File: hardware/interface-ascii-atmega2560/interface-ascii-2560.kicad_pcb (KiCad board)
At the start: 2 copper layers, 88.9 x 132.1 mm, 50 parts, among them J1 Apple 2, J10 Keyboard, J2 Apple 1, J3 UART, J4 Conn_01x05, J5 SOL-20, J6 Program, J7 Custom Connector 1 / Proto, J8 Conn_01x25, SW1 Options, U1 ATmega2560-16AU, Y1 16.000 MHz

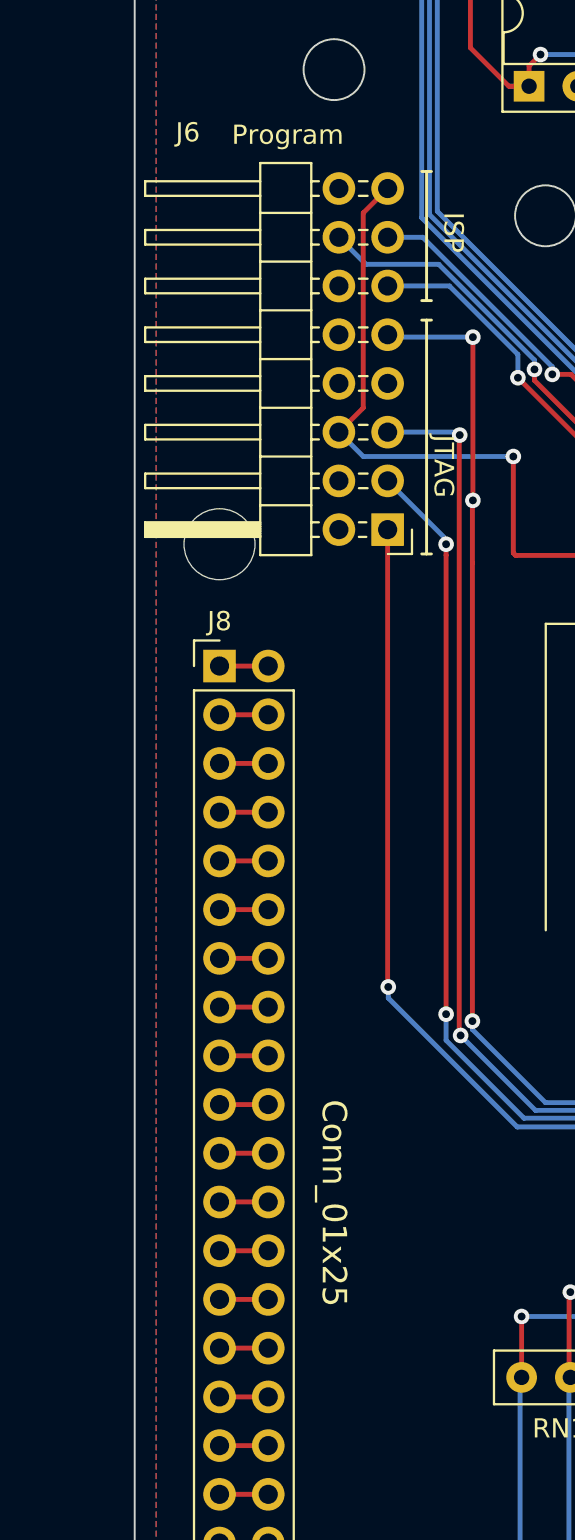
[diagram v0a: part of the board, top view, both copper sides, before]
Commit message: Fix connector J8 name to "custom connector 2"
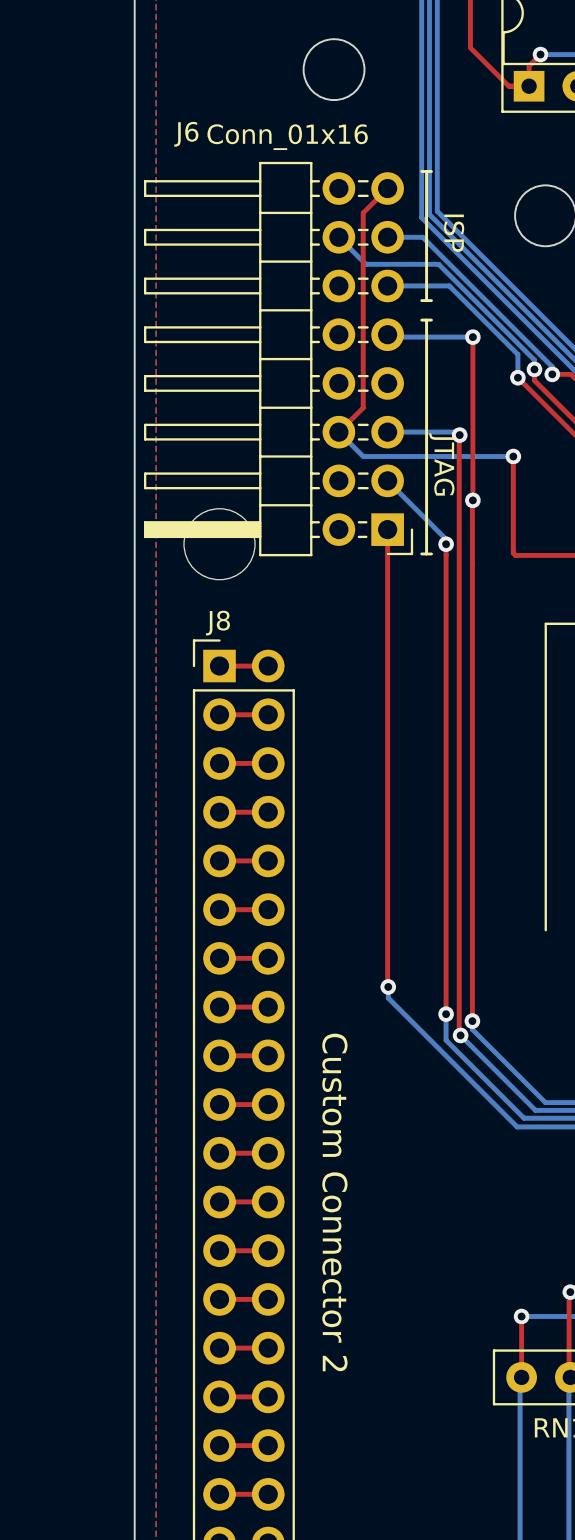
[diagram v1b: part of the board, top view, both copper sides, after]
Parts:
- J6: value Program -> Conn_01x16
- J8: value Conn_01x25 -> Custom Connector 2
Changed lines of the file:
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@@
       (effects (font (size 1 1) (thickness 0.15)))
     )
-    (fp_text value Program (at 5.207 20.574) (layer F.SilkS)
+    (fp_text value Conn_01x16 (at 5.207 20.574) (layer F.SilkS)
       (effects (font (size 1 1) (thickness 0.15)))
     )
@@
       (effects (font (size 1 1) (thickness 0.15)))
     )
-    (fp_text value Conn_01x25 (at 5.969 28.0035 270 unlocked) (layer F.SilkS)
+    (fp_text value "Custom Connector 2" (at 5.969 28.0035 270 unlocked) (layer F.SilkS)
       (effects (font (size 1.27 1.27) (thickness 0.15)))
     )

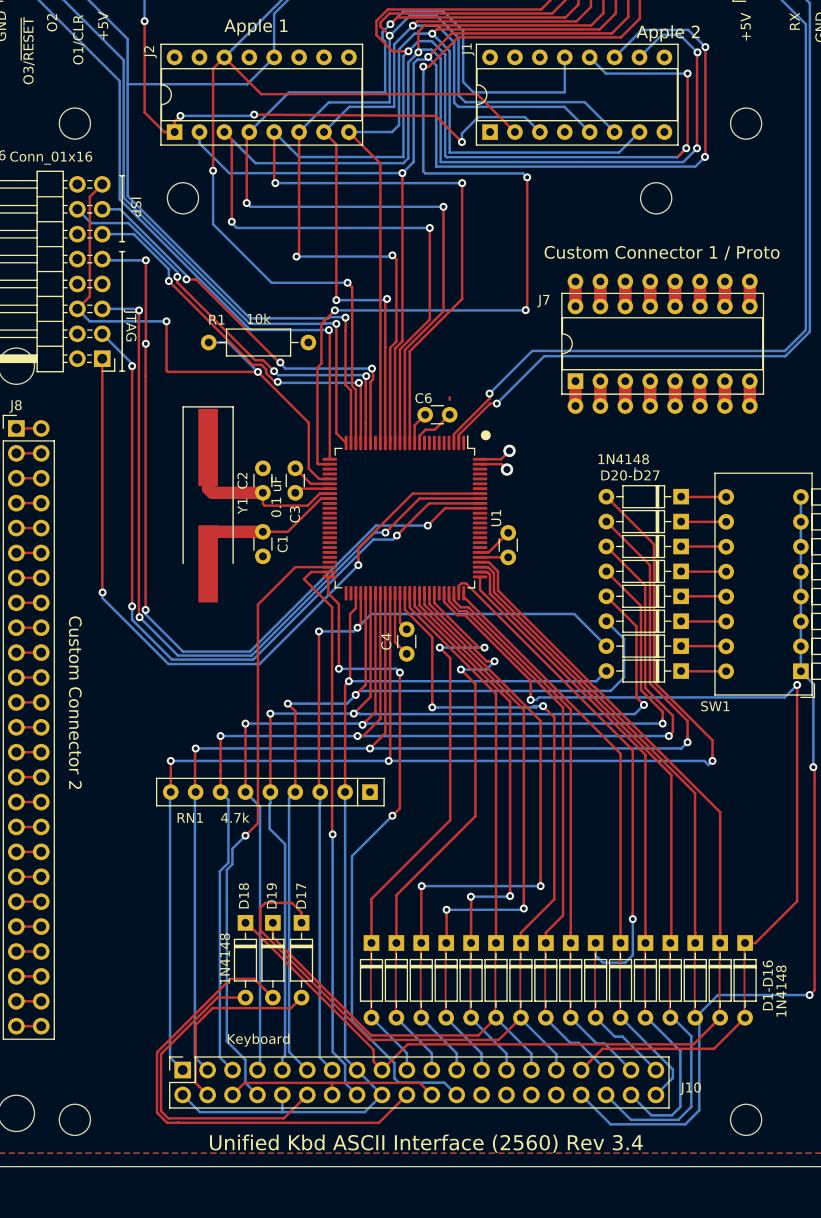
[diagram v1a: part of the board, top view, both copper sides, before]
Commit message: mechanical fit and buildability fixes
- Moved header slightly forward

- Moved interface mount holes do reduce interference with case mount holes

- For all keys in classic keyboard, add option for either through-hole or SMT
diodes and resistors.
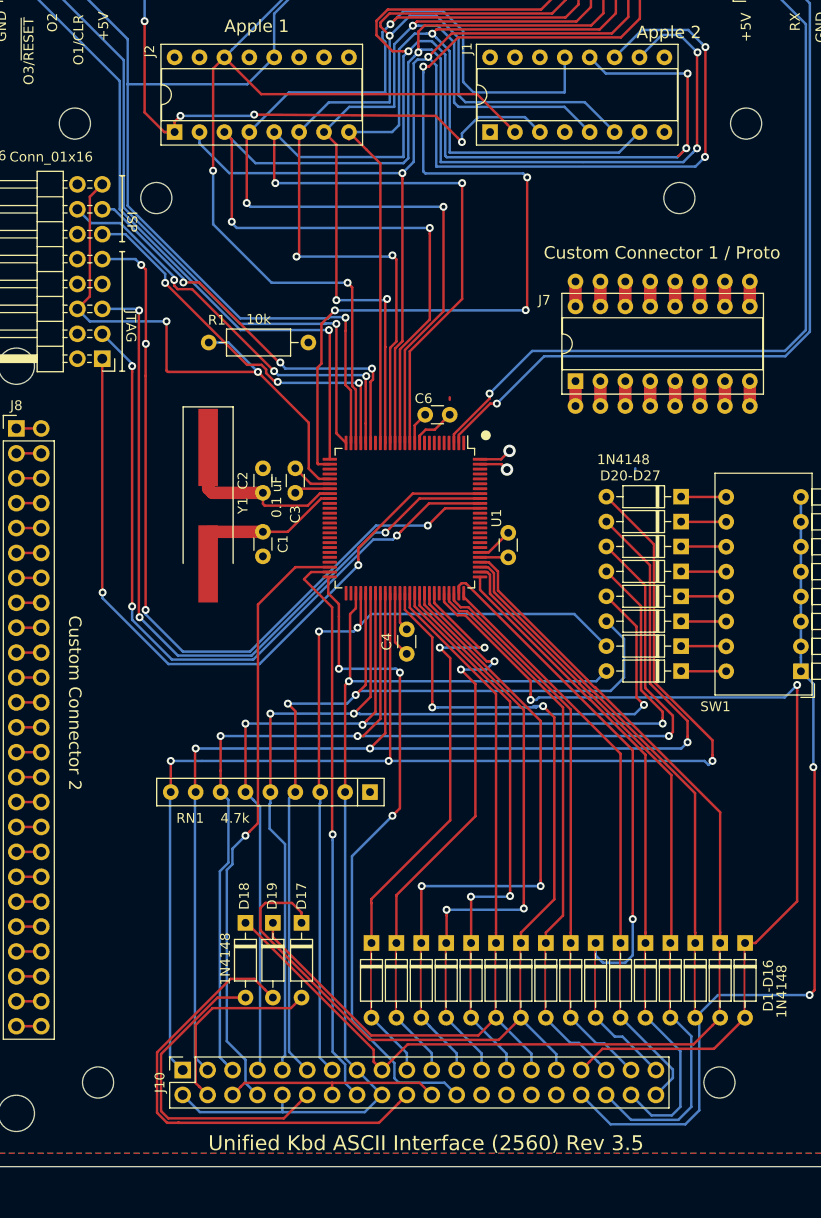
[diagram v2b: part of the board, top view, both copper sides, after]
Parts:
- J10: footprint unikbd:PinHeader_2x20_P2.54mm_Vertical -> unikbd:kbd_header_and_mounting_holes
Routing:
- net /OUT3: track 184.0 -> 184.6 mm
- net /OUT2: track 114.7 -> 115.3 mm
- net /OUT1: track 122.7 -> 123.2 mm
- net /TDI: track 82.4 -> 81.8 mm
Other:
- outline, holes or cut-outs redrawn
- board text added: "Unified Kbd ASCII Interface (2560) Rev 3.5"
- board text removed: "Mounting holes: 0.125" Non-plated 2.5" square spacing Pin 1 of connector 0.31", 0" (x,y) relative to center of left lower hole."
- board text removed: "Pin 1 of keyboard connector must be at least 3.5" from pin 1 of interface connector in order for interface connector to be accessible with keyboard assembled."
- board text removed: "Unified Kbd ASCII Interface (2560) Rev 3.4"

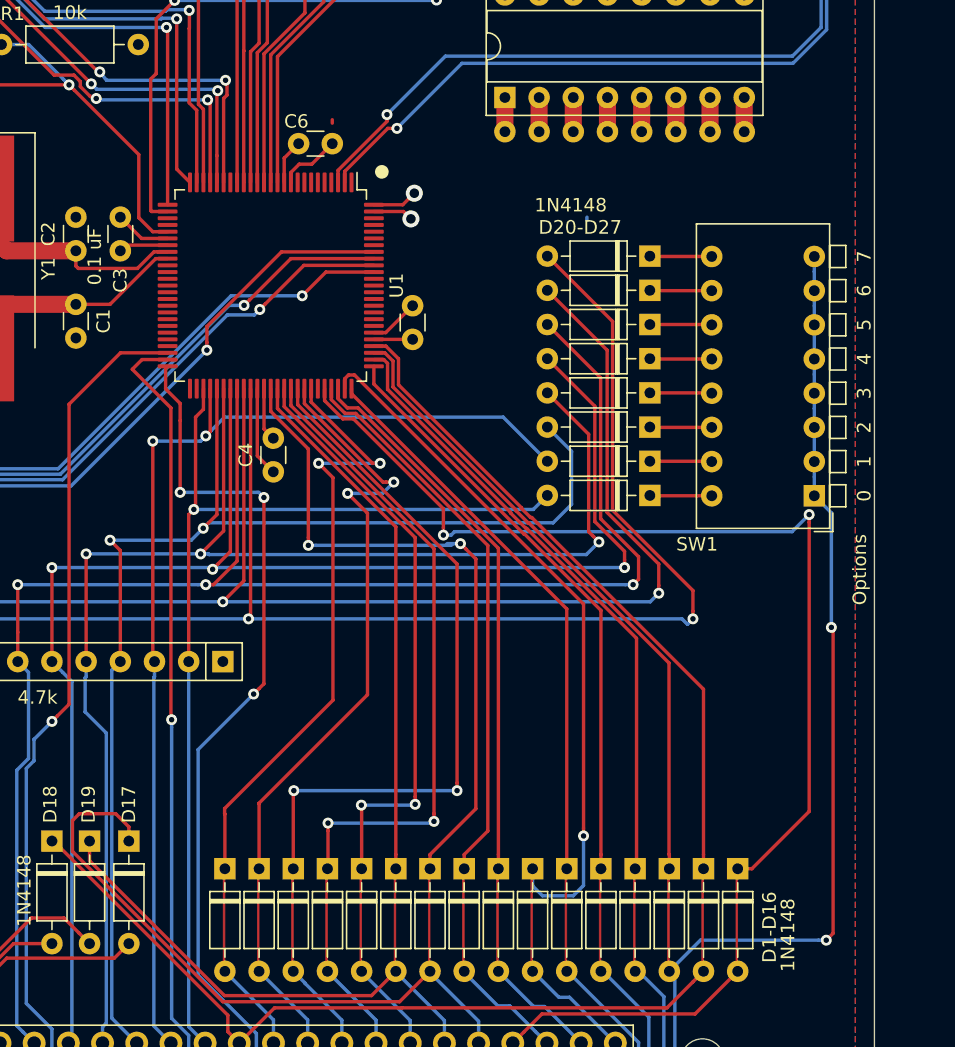
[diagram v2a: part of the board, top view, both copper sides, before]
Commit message: Modify to use DIP switch or jumpers
- Add combined DIP-switch/Jumper footprint to footprint library
- Fix Apple2-encoder and interface-ascii-atmega2560 schematics and PCB to use
new footprint.
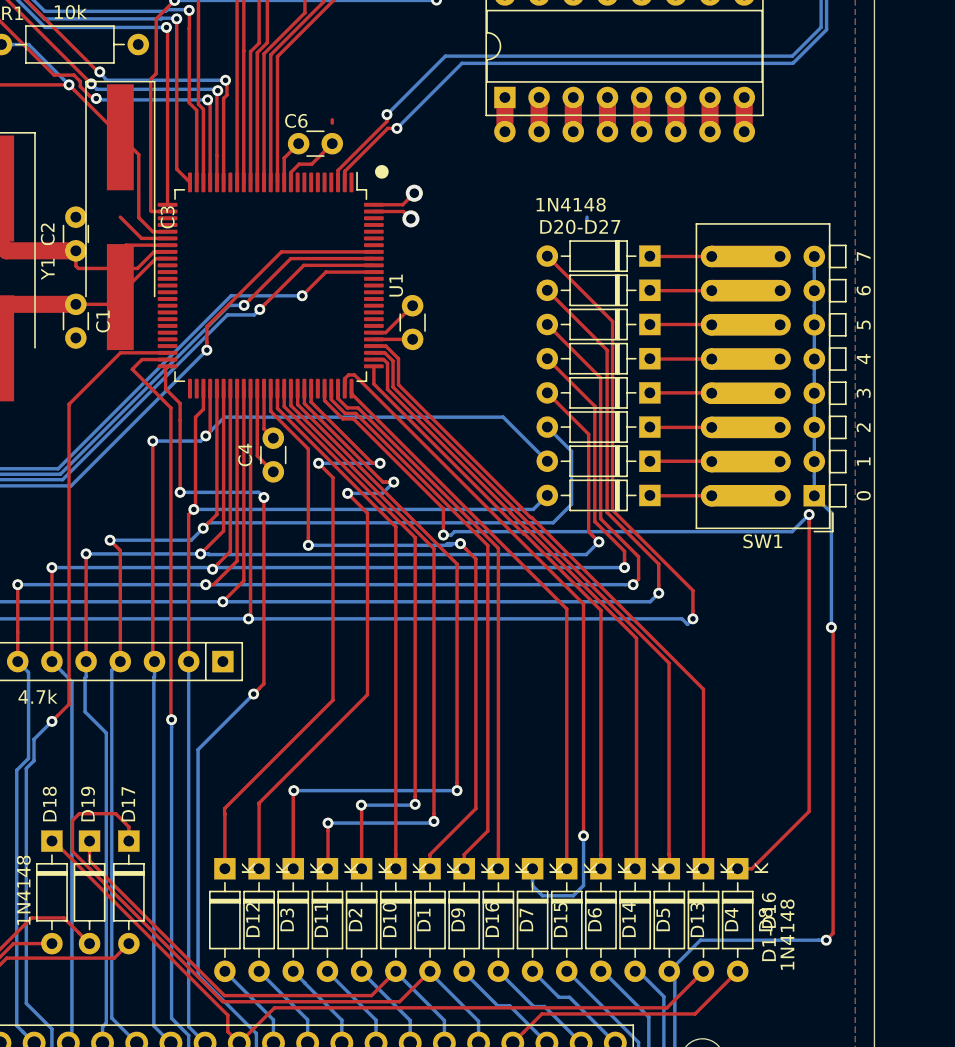
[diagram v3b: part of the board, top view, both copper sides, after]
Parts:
- C3: footprint Capacitor_THT:C_Disc_D3.0mm_W1.6mm_P2.50mm -> Crystal:Crystal_SMD_HC49-SD_HandSoldering
- D1, D10, D11, D12, D13, D14, D15, D16, D2, D3, D4, D5, D6, D7, D8, D9: footprint unikbd:D_DO-35_SOD27_P7.62mm_Horizontal_bypassed -> Diode_THT:D_DO-35_SOD27_P7.62mm_Horizontal
- SW1: footprint Button_Switch_THT:SW_DIP_SPSTx08_Piano_CTS_Series194-8MSTN_W7.62mm_P2.54mm -> unikbd:SW_DIP_SPSTx08_Piano_CTS_Series194-8MSTN_W7.62mm_P2.54mm

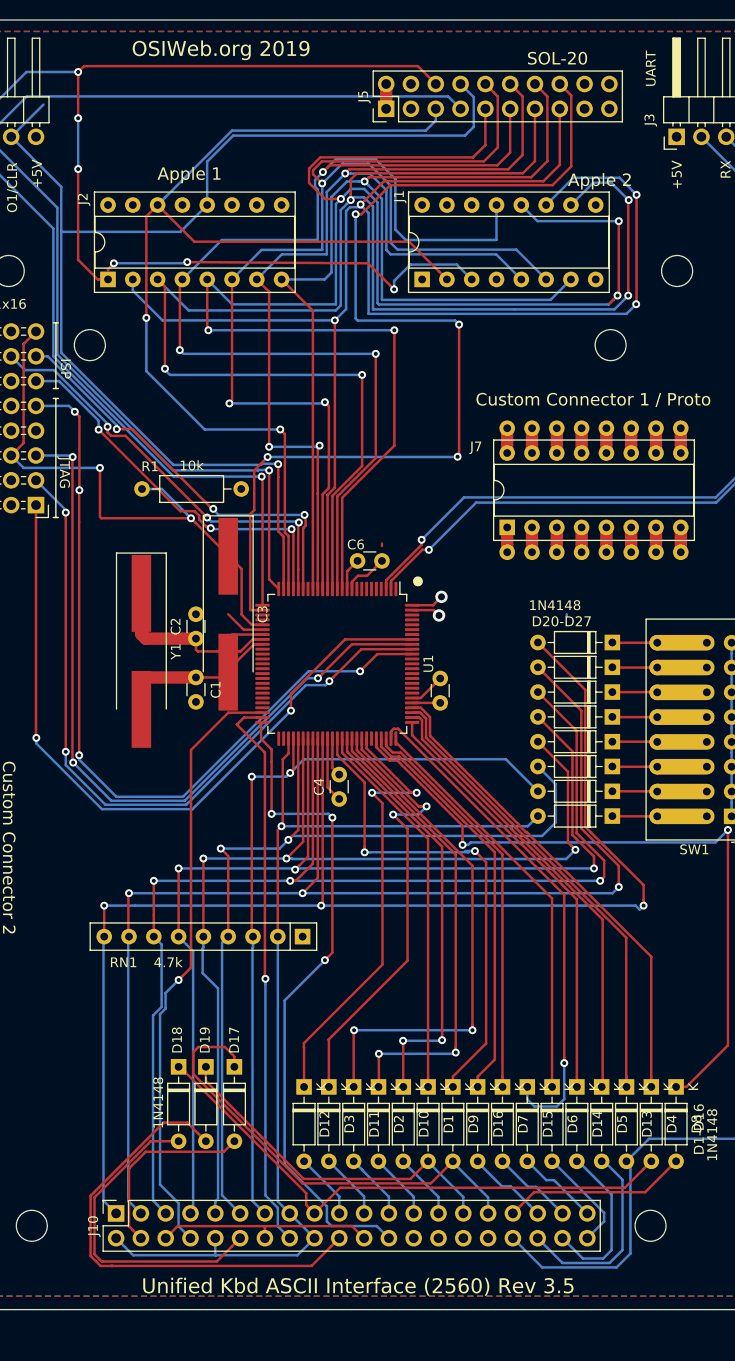
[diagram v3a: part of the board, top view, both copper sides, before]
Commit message: Fix shunted diode footprints on encoder boards
The encoder boards (ATmega328P, Atmega2560, Apple2(2560) can accomodate
keyboard matrices with no diodes, by adding per-row diodes on the
encoder board.  For keyboards with per-key diodes (the typical use
case), the per-row diodes are not needed, and therefore the footprints
should be shunted by default, using a special shunted diode footprint.
When diodes are installed, the shunt can be cut with an x-acto knife.
Previous board revs had the correct footprint, but somehow the regular
diode footprint was substituted on the last release of each of these
PCBS.  The correct footprint has been restored.
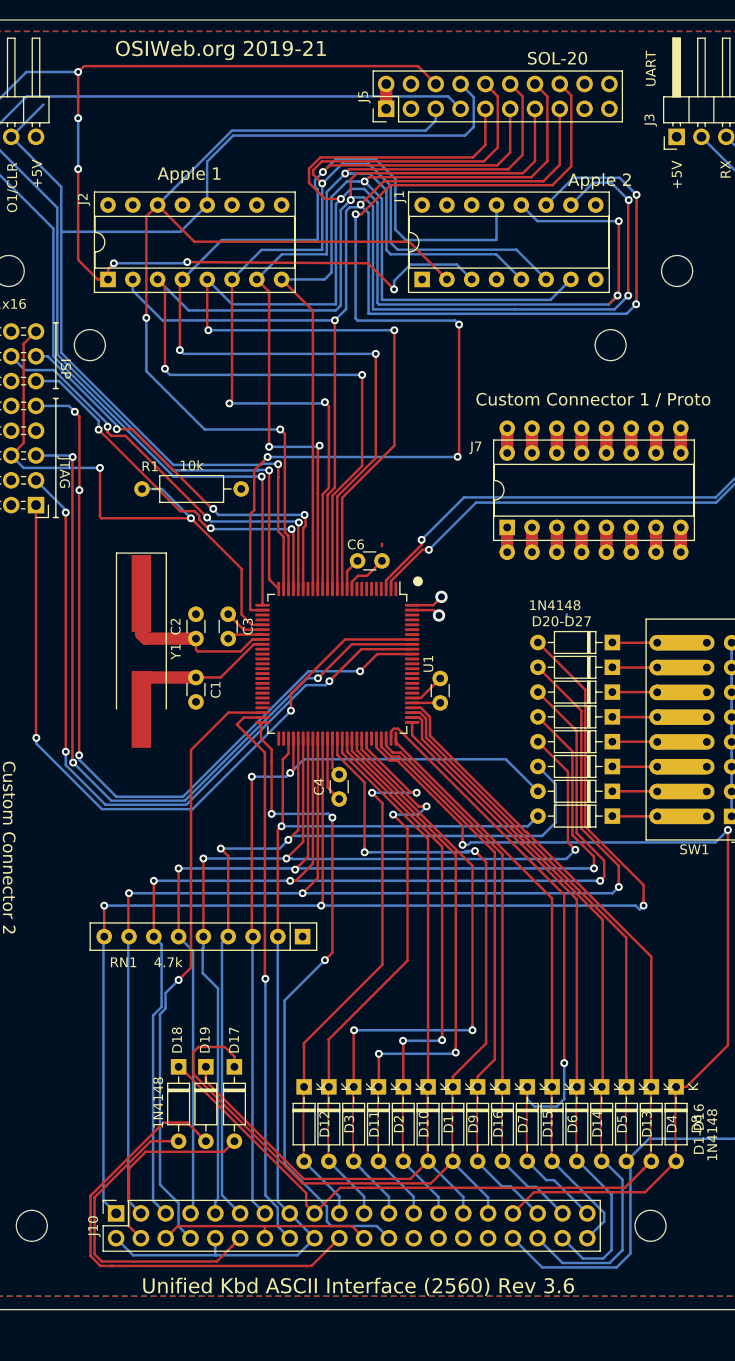
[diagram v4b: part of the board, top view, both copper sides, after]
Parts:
- C3: footprint Crystal:Crystal_SMD_HC49-SD_HandSoldering -> Capacitor_THT:C_Disc_D3.0mm_W1.6mm_P2.50mm
- D1, D10, D11, D12, D13, D14, D15, D16, D2, D3, D4, D5, D6, D7, D8, D9: footprint Diode_THT:D_DO-35_SOD27_P7.62mm_Horizontal -> unikbd:D_DO-35_SOD27_P7.62mm_Horizontal_bypassed
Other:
- board text added: "OSIWeb.org 2019-21"
- board text added: "Unified Kbd ASCII Interface (2560) Rev 3.6"
- board text removed: "OSIWeb.org 2019"
- board text removed: "Unified Kbd ASCII Interface (2560) Rev 3.5"
